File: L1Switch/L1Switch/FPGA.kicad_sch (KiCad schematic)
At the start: 6 parts, among them U1 XC7A15T-FTG256

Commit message: Most signals routed.
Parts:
- added J11: Conn_01x06_Male, Connector_PinHeader_2.54mm:PinHeader_1x06_P2.54mm_Vertical, symbol Connector:Conn_01x06_Male
- added TP1: TestPoint, TestPoint:TestPoint_Pad_1.0x1.0mm, symbol Connector:TestPoint
- added X1: LFSPXO076034CUTT, L1Switch:LFSPXO076034, symbol Oscillator:ASE-xxxMHz
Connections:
- net +1V2: now also X1.1 (EN), X1.4 (Vdd)
- net SGMII2.RD_N6: now also U1.J16 (IO_L23N_T3_FWE_B_15); no longer U1.M15 (IO_L3N_T0_DQS_EMCCLK_14)
- net SGMII2.RD_N7: now also U1.G16 (IO_L22N_T3_A16_15); no longer U1.K16 (IO_L2N_T0_D03_14)
- net SGMII2.RD_P6: now also U1.J15 (IO_L23P_T3_FOE_B_15); no longer U1.L15 (IO_L3P_T0_DQS_PUDC_B_14)
- net SGMII2.RD_P7: now also U1.H16 (IO_L22P_T3_A17_15); no longer U1.K15 (IO_L2P_T0_D02_14)
- net SGMII2.TD_N4: now also U1.L13 (IO_L5N_T0_D07_14); no longer U1.M12 (IO_L6N_T0_D08_VREF_14)
- net SGMII2.TD_N5: now also U1.M14 (IO_L4N_T0_D05_14); no longer U1.L13 (IO_L5N_T0_D07_14)
- net SGMII2.TD_N6: now also U1.G12 (IO_L19N_T3_A21_VREF_15); no longer U1.M14 (IO_L4N_T0_D05_14)
- net SGMII2.TD_N7: now also U1.H13 (IO_L20N_T3_A19_15); no longer U1.J14 (IO_L1N_T0_D01_DIN_14)
- net SGMII2.TD_P4: now also U1.K13 (IO_L5P_T0_D06_14); no longer U1.L12 (IO_L6P_T0_FCS_B_14)
- net SGMII2.TD_P5: now also U1.L14 (IO_L4P_T0_D04_14); no longer U1.K13 (IO_L5P_T0_D06_14)
- net SGMII2.TD_P6: now also U1.H11 (IO_L19P_T3_A22_15); no longer U1.L14 (IO_L4P_T0_D04_14)
- net SGMII2.TD_P7: now also U1.H12 (IO_L20P_T3_A20_15); no longer U1.J13 (IO_L1P_T0_D00_MOSI_14)
- net FPGA_TXD: now reaches U1.T3 (IO_L9N_T1_DQS_34)
- net FPGA_TXD: now also J11.4 (Pin_4)
- net FPGA_RXD: now reaches U1.T4 (IO_L9P_T1_DQS_34)
- net FPGA_RXD: now also J11.5 (Pin_5)
- net SGMII3.RD_N7: now reaches U1.A10 (IO_L3N_T0_DQS_AD1N_15)
- net SGMII3.RD_N5: now reaches U1.A12 (IO_L5N_T0_AD9N_15)
- net SGMII3.RD_P4: now reaches U1.A13 (IO_L7P_T1_AD2P_15)
- net SGMII3.RD_N4: now reaches U1.A14 (IO_L7N_T1_AD2N_15)
- net SGMII3.RD_N3: now reaches U1.A15 (IO_L9N_T1_DQS_AD3N_15)
- net SGMII3.TD_P7: now reaches U1.A8 (IO_L2P_T0_AD8P_15)
- net SGMII3.TD_N7: now reaches U1.A9 (IO_L2N_T0_AD8N_15)
- net SGMII3.RD_P6: now reaches U1.B10 (IO_L4P_T0_15)
- net SGMII3.RD_N6: now reaches U1.B11 (IO_L4N_T0_15)
- net SGMII3.RD_P5: now reaches U1.B12 (IO_L5P_T0_AD9P_15)
- net SGMII3.RD_P3: now reaches U1.B15 (IO_L9P_T1_DQS_AD3P_15)
- net SGMII3.RD_N2: now reaches U1.B16 (IO_L10N_T1_AD11N_15)
- net SGMII3.RD_P7: now reaches U1.B9 (IO_L3P_T0_DQS_AD1P_15)
- net SGMII3.RD_P2: now reaches U1.C16 (IO_L10P_T1_AD11P_15)
- net SGMII3.TD_P6: now reaches U1.C8 (IO_L1P_T0_AD0P_15)
- net SGMII3.TD_N6: now reaches U1.C9 (IO_L1N_T0_AD0N_15)
- net SGMII3.TD_N4: now reaches U1.D11 (IO_L14N_T2_SRCC_15)
- net CLK_25: now reaches U1.D13 (IO_L12P_T1_MRCC_15)
- net CLK_25: now also TP1.1, X1.3 (OUT)
- net SGMII3.TD_P3: now reaches U1.D14 (IO_L15P_T2_DQS_15)
- net SGMII3.TD_N3: now reaches U1.D15 (IO_L15N_T2_DQS_ADV_B_15)
- net SGMII3.RD_N1: now reaches U1.D16 (IO_L17N_T2_A25_15)
- net SGMII3.TD_P5: now reaches U1.D8 (IO_L6P_T0_15)
- net SGMII3.TD_N5: now reaches U1.D9 (IO_L6N_T0_VREF_15)
- net SGMII3.TD_P4: now reaches U1.E11 (IO_L14P_T2_SRCC_15)
- net SGMII3.RD_N0: now reaches U1.E15 (IO_L18N_T2_A23_15)
- net SGMII3.RD_P1: now reaches U1.E16 (IO_L17P_T2_A26_15)
- net SGMII3.TD_P2: now reaches U1.F12 (IO_L16P_T2_A28_15)
- net SGMII3.TD_N2: now reaches U1.F13 (IO_L16N_T2_A27_15)
- net SGMII3.TD_N1: now reaches U1.F14 (IO_L21N_T3_DQS_A18_15)
- net SGMII3.RD_P0: now reaches U1.F15 (IO_L18P_T2_A24_15)
- net SGMII3.TD_P1: now reaches U1.G14 (IO_L21P_T3_DQS_15)
- net SGMII3.TD_N0: now reaches U1.G15 (IO_L24N_T3_RS0_15)
- net SGMII3.TD_P0: now reaches U1.H14 (IO_L24P_T3_RS1_15)
- new net CS_N: U1.L12 (IO_L6P_T0_FCS_B_14)
- new net DI: U1.J13 (IO_L1P_T0_D00_MOSI_14)
- new net DO: U1.J14 (IO_L1N_T0_D01_DIN_14)
- new net GND: J11.1 (Pin_1), U1.L15 (IO_L3P_T0_DQS_PUDC_B_14), X1.2 (GND)
- new net HOLD_N: U1.K16 (IO_L2N_T0_D03_14)
- new net W_N: U1.K15 (IO_L2P_T0_D02_14)
- no-connect marks 3 -> 22

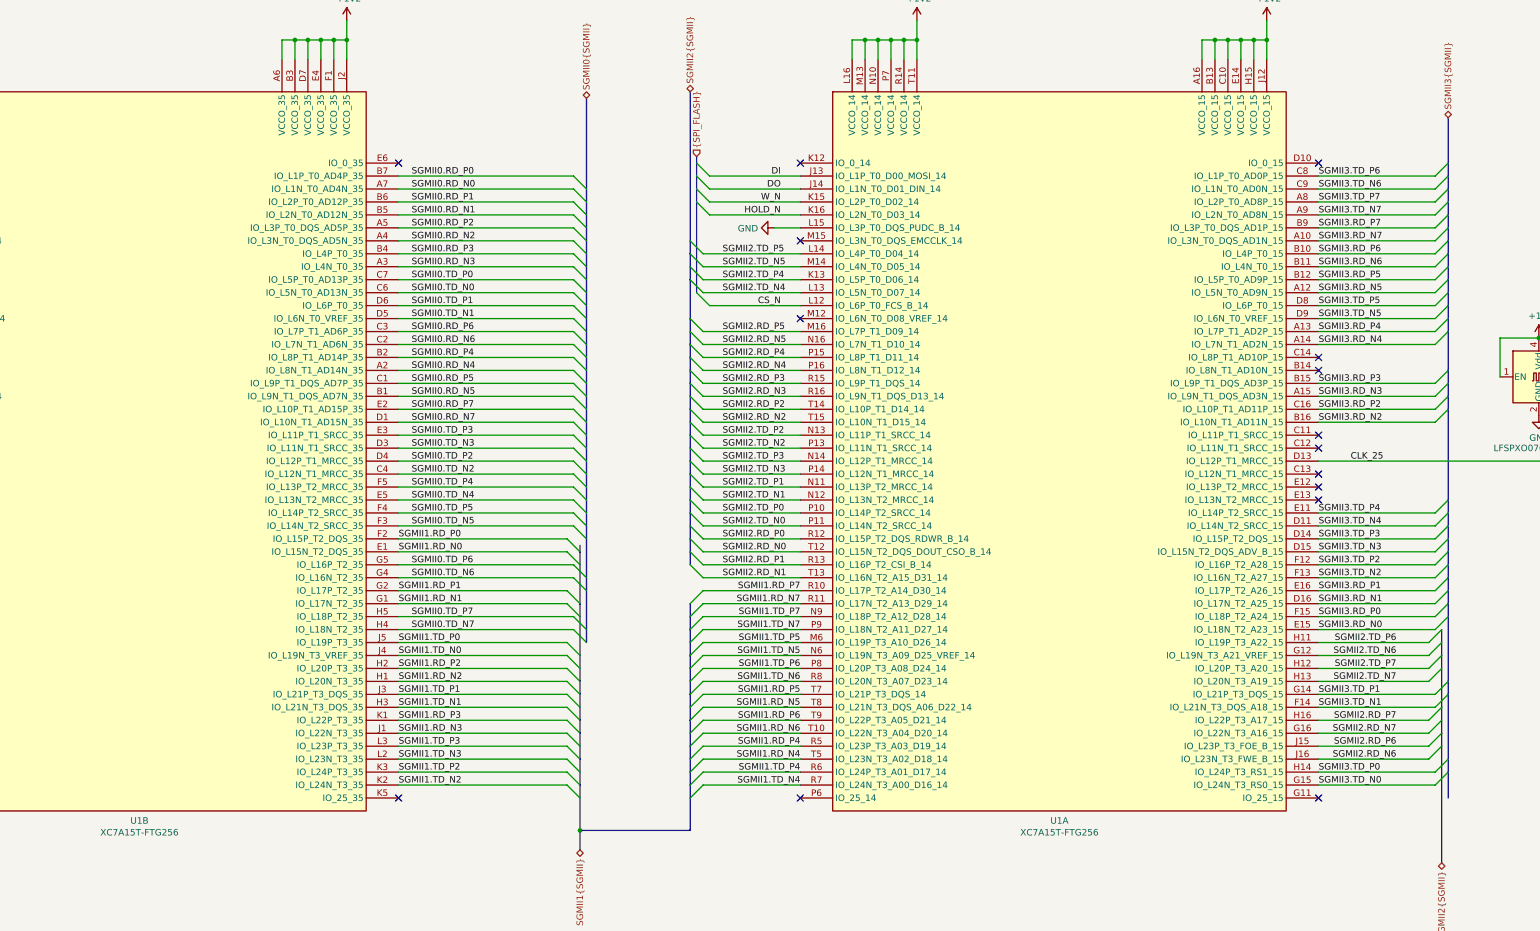
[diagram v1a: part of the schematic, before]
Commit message: Switch to XC7A35T. Update some layout constraints for 4pcb.com capabilities.
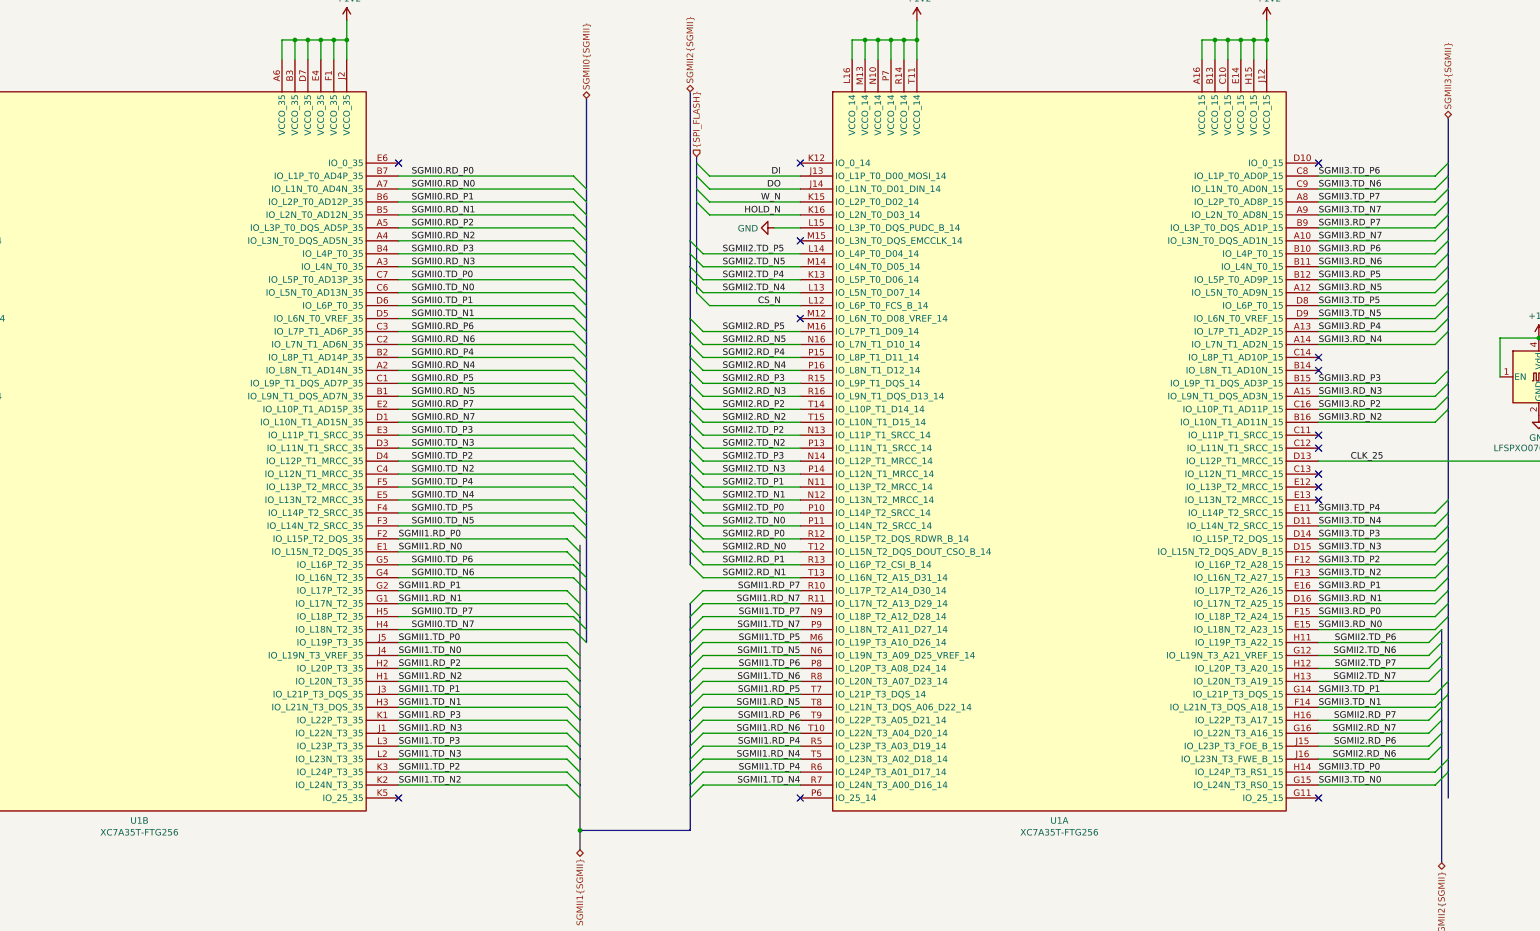
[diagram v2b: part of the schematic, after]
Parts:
- U1: value XC7A15T-FTG256 -> XC7A35T-FTG256; symbol FPGA_Xilinx_Artix7:XC7A15T-FTG256 -> FPGA_Xilinx_Artix7:XC7A35T-FTG256

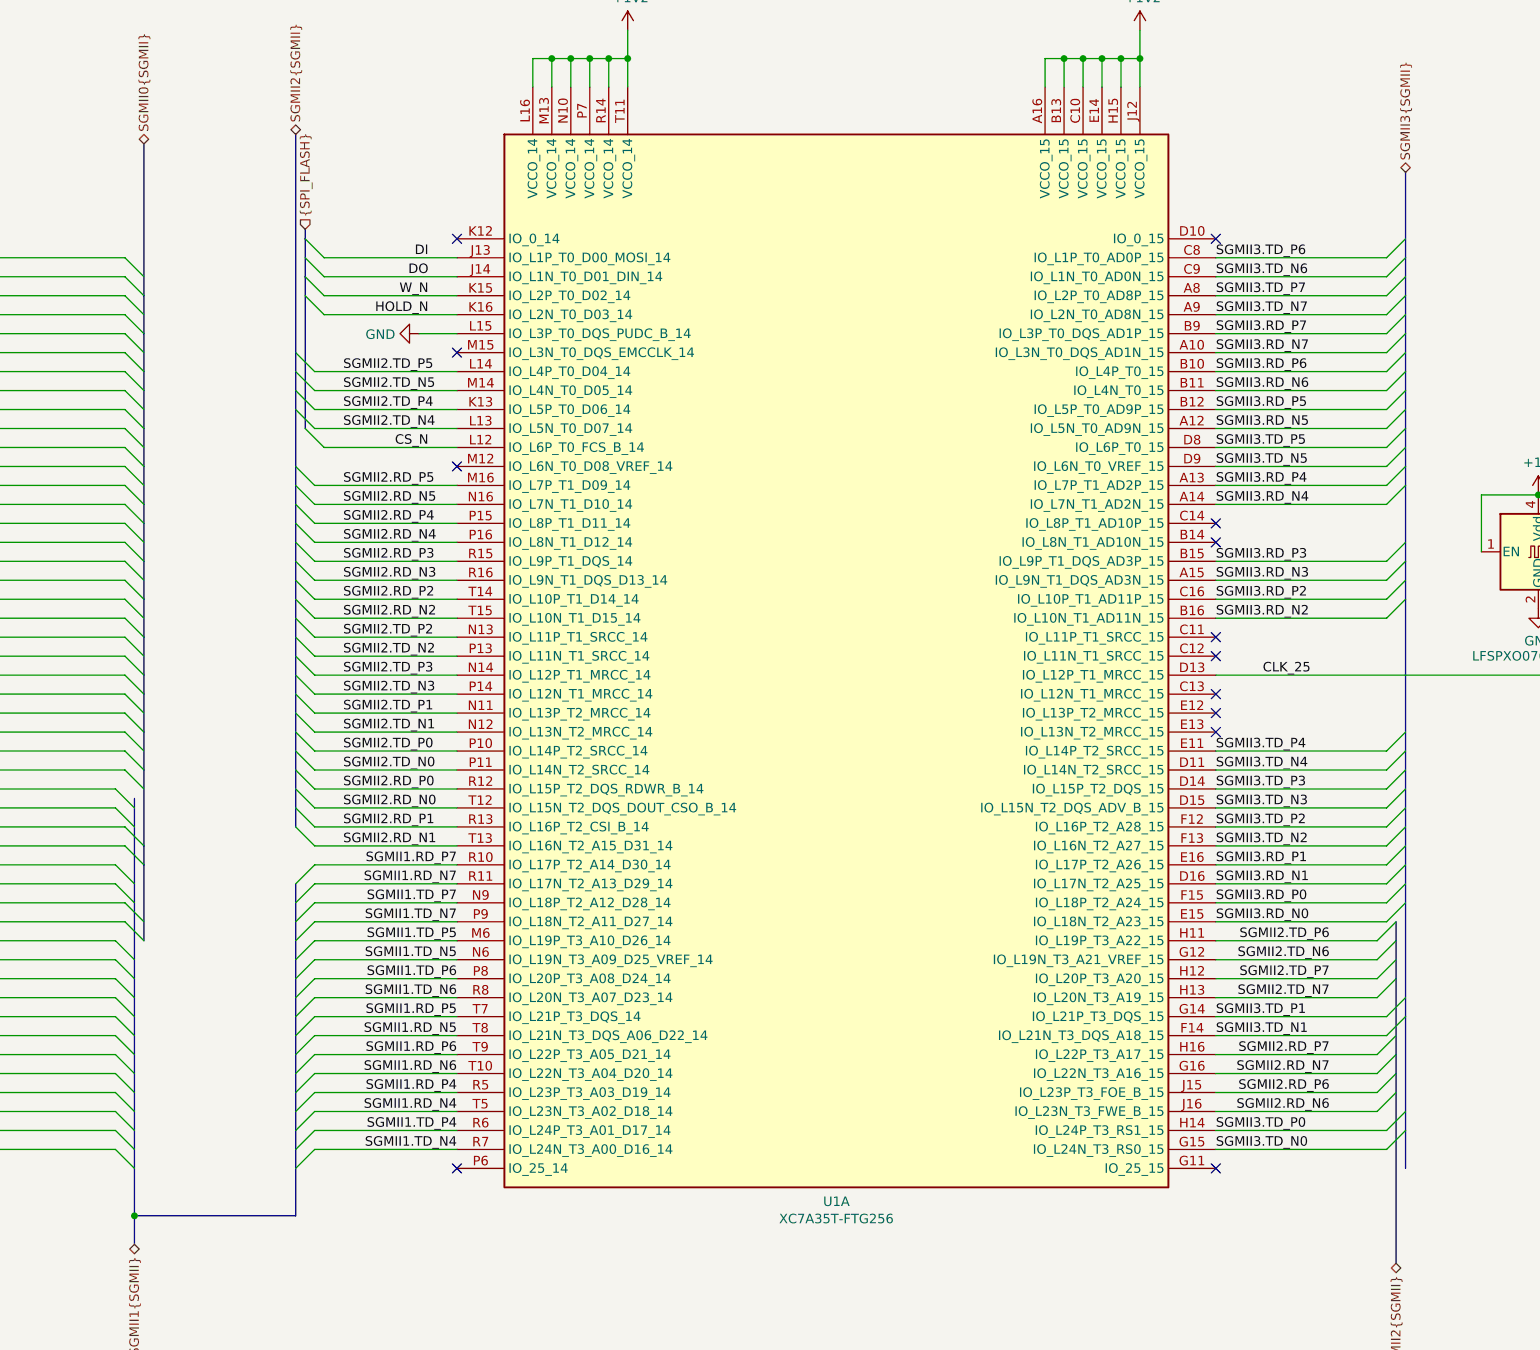
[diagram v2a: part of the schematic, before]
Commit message: Added return path vias. Updated all paths for spacing.
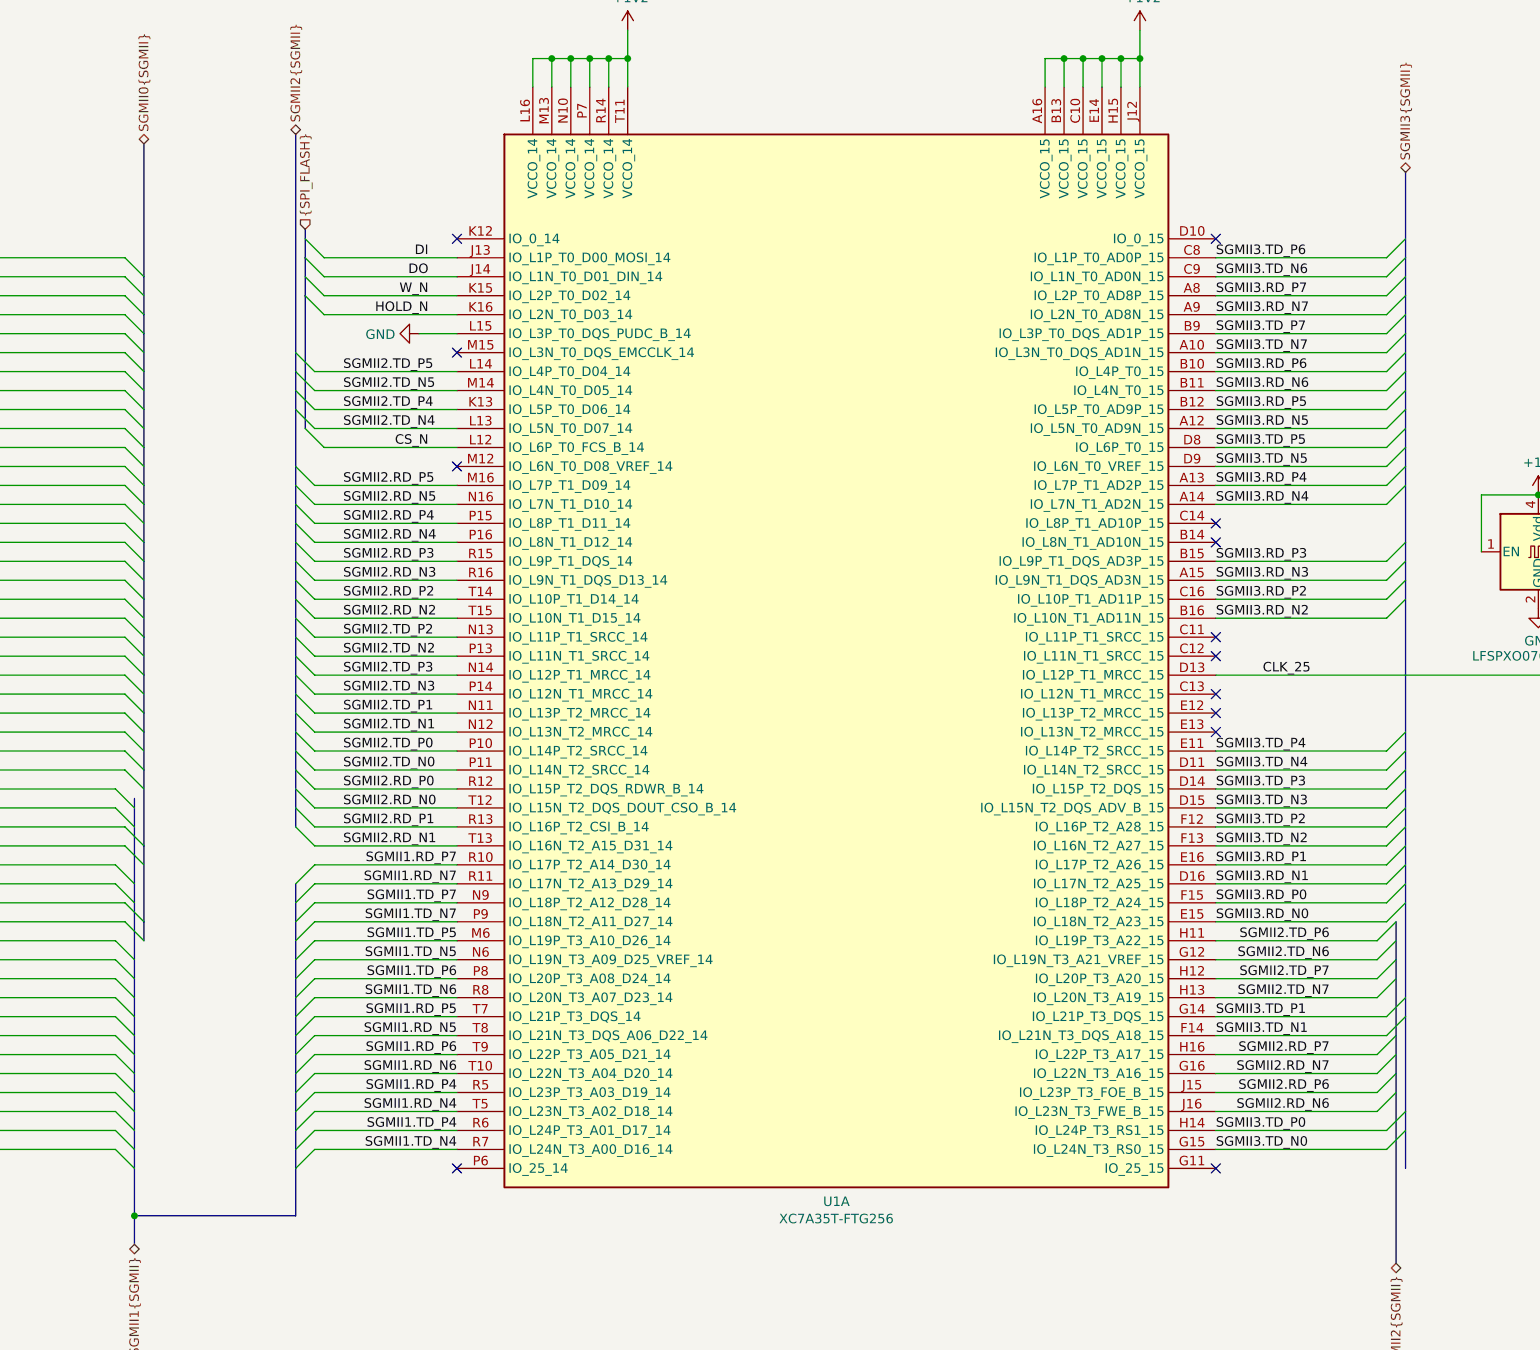
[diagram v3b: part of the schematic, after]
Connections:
- net SGMII3.RD_N7: now also U1.A9 (IO_L2N_T0_AD8N_15); no longer U1.A10 (IO_L3N_T0_DQS_AD1N_15)
- net SGMII3.RD_P7: now also U1.A8 (IO_L2P_T0_AD8P_15); no longer U1.B9 (IO_L3P_T0_DQS_AD1P_15)
- net SGMII3.TD_N7: now also U1.A10 (IO_L3N_T0_DQS_AD1N_15); no longer U1.A9 (IO_L2N_T0_AD8N_15)
- net SGMII3.TD_P7: now also U1.B9 (IO_L3P_T0_DQS_AD1P_15); no longer U1.A8 (IO_L2P_T0_AD8P_15)
